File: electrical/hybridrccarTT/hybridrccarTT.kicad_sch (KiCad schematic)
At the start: 0 parts

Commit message: river the goat
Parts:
- added U1: STM32F103C8Tx, Package_QFP:LQFP-48_7x7mm_P0.5mm, symbol MCU_ST_STM32F1:STM32F103C8Tx
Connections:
- new net: U1.23 (VSS), U1.35 (VSS), U1.47 (VSS)
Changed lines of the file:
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@@
+		)
+	)
+	(symbol
+		(lib_id "MCU_ST_STM32F1:STM32F103C8Tx")
+		(at 76.2 97.79 0)
+		(unit 1)
+		(exclude_from_sim no)
+		(in_bom yes)
+		(on_board yes)
+		(dnp no)
+		(fields_autoplaced yes)
+		(property "Reference" "U1"
+			(at 80.8833 138.43 0)
+			(effects
+				(font
+					(size 1.27 1.27)
+				)
+				(justify left)
+			)
+		)
+		(property "Value" "STM32F103C8Tx"
+			(at 80.8833 140.97 0)
+			(effects
+				(font
+					(size 1.27 1.27)
+				)
+				(justify left)
+			)
+		)
+		(property "Footprint" "Package_QFP:LQFP-48_7x7mm_P0.5mm"
+			(at 60.96 135.89 0)
+			(effects
+				(font
+					(size 1.27 1.27)
+				)
+				(justify right)
+				(hide yes)
+			)
+		)
+		(property "Datasheet" "https://www.st.com/resource/en/datasheet/stm32f103c8.pdf"
+			(at 76.2 97.79 0)
+			(effects
+				(font
+					(size 1.27 1.27)
+				)
+				(hide yes)
+			)
+		)
+		(property "Description" "STMicroelectronics Arm Cortex-M3 MCU, 64KB flash, 20KB RAM, 72 MHz, 2.0-3.6V, 37 GPIO, LQFP48"
+			(at 76.2 97.79 0)
+			(effects
+				(font
+					(size 1.27 1.27)
+				)
+				(hide yes)
+			)
+		)
+		(pin "16"
+		)
+		(pin "15"
+		)
+		(pin "14"
+		)
+		(pin "13"
+		)
+		(pin "12"
+		)
+		(pin "11"
+		)
+		(pin "10"
+		)
+		(pin "34"
+		)
+		(pin "33"
+		)
+		(pin "32"
+		)
+		(pin "31"
+		)
+		(pin "30"
+		)
+		(pin "9"
+		)
+		(pin "47"
+		)
+		(pin "48"
+		)
+		(pin "8"
+		)
+		(pin "29"
+		)
+		(pin "17"
+		)
+		(pin "37"
+		)
+		(pin "38"
+		)
+		(pin "43"
+		)
+		(pin "45"
+		)
+		(pin "46"
+		)
+		(pin "3"
+		)
+		(pin "4"
+		)
+		(pin "18"
+		)
+		(pin "19"
+		)
+		(pin "20"
+		)
+		(pin "39"
+		)
+		(pin "40"
+		)
+		(pin "41"
+		)
+		(pin "1"
+		)
+		(pin "28"
+		)
+		(pin "27"
+		)
+		(pin "26"
+		)
+		(pin "25"
+		)
+		(pin "22"
+		)
+		(pin "21"
+		)
+		(pin "7"
+		)
+		(pin "44"
+		)
+		(pin "5"
+		)
+		(pin "6"
+		)
+		(pin "2"
+		)
+		(pin "42"
+		)
+		(pin "24"
+		)
+		(pin "36"
+		)
+		(pin "23"
+		)
+		(pin "35"
+		)
+		(instances
+			(project ""
+				(path "/d3b268c2-36da-438c-a1fa-ee4bf32aa038"
+					(reference "U1")
+					(unit 1)
+				)
+			)
 		)
 	)

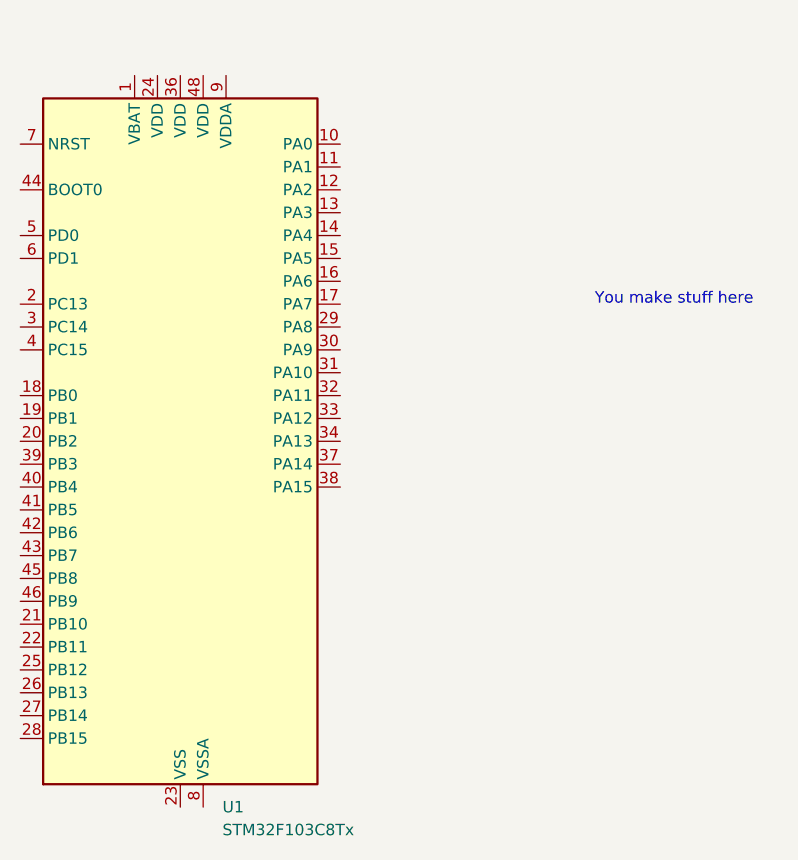
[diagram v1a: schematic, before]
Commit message: added stm32 lib
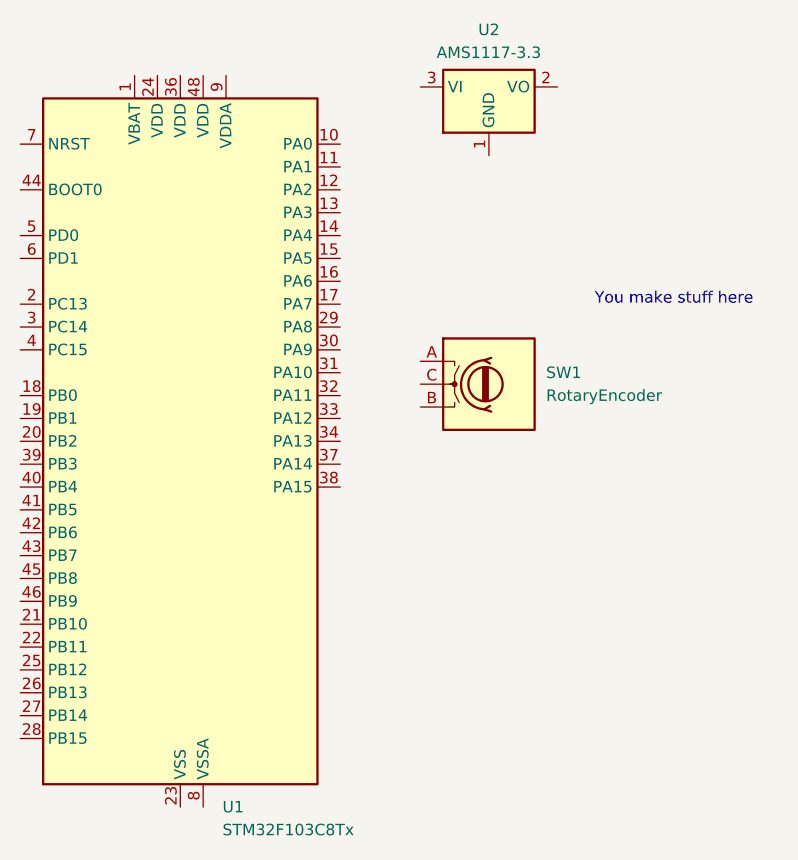
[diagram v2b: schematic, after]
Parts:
- added SW1: RotaryEncoder, symbol Device:RotaryEncoder
- added U2: AMS1117-3.3, Package_TO_SOT_SMD:SOT-223-3_TabPin2, symbol Regulator_Linear:AMS1117-3.3
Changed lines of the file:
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@@
+	)
+	(symbol
+		(lib_id "Device:RotaryEncoder")
+		(at 110.49 91.44 0)
+		(unit 1)
+		(exclude_from_sim no)
+		(in_bom yes)
+		(on_board yes)
+		(dnp no)
+		(fields_autoplaced yes)
+		(property "Reference" "SW1"
+			(at 116.84 90.1699 0)
+			(effects
+				(font
+					(size 1.27 1.27)
+				)
+				(justify left)
+			)
+		)
+		(property "Value" "RotaryEncoder"
+			(at 116.84 92.7099 0)
+			(effects
+				(font
+					(size 1.27 1.27)
+				)
+				(justify left)
+			)
+		)
+		(property "Footprint" ""
+			(at 106.68 87.376 0)
+			(effects
+				(font
+					(size 1.27 1.27)
+				)
+				(hide yes)
+			)
+		)
+		(property "Datasheet" "~"
+			(at 110.49 84.836 0)
+			(effects
+				(font
+					(size 1.27 1.27)
+				)
+				(hide yes)
+			)
+		)
+		(property "Description" "Rotary encoder, dual channel, incremental quadrate outputs"
+			(at 110.49 91.44 0)
+			(effects
+				(font
+					(size 1.27 1.27)
+				)
+				(hide yes)
+			)
+		)
+		(pin "A"
+		)
+		(pin "B"
+		)
+		(pin "C"
+		)
+		(instances
+			(project ""
+				(path "/d3b268c2-36da-438c-a1fa-ee4bf32aa038"
+					(reference "SW1")
+					(unit 1)
+				)
+			)
+		)
+	)
+	(symbol
+		(lib_id "Regulator_Linear:AMS1117-3.3")
+		(at 110.49 58.42 0)
+		(unit 1)
+		(exclude_from_sim no)
+		(in_bom yes)
+		(on_board yes)
+		(dnp no)
+		(fields_autoplaced yes)
+		(property "Reference" "U2"
+			(at 110.49 52.07 0)
+			(effects
+				(font
+					(size 1.27 1.27)
+				)
+			)
+		)
+		(property "Value" "AMS1117-3.3"
+			(at 110.49 54.61 0)
+			(effects
+				(font
+					(size 1.27 1.27)
+				)
+			)
+		)
+		(property "Footprint" "Package_TO_SOT_SMD:SOT-223-3_TabPin2"
+			(at 110.49 53.34 0)
+			(effects
+				(font
+					(size 1.27 1.27)
+				)
+				(hide yes)
+			)
+		)
+		(property "Datasheet" "http://www.advanced-monolithic.com/pdf/ds1117.pdf"
+			(at 113.03 64.77 0)
+			(effects
+				(font
+					(size 1.27 1.27)
+				)
+				(hide yes)
+			)
+		)
+		(property "Description" "1A Low Dropout regulator, positive, 3.3V fixed output, SOT-223"
+			(at 110.49 58.42 0)
+			(effects
+				(font
+					(size 1.27 1.27)
+				)
+				(hide yes)
+			)
+		)
+		(pin "3"
+		)
+		(pin "2"
+		)
+		(pin "1"
+		)
+		(instances
+			(project ""
+				(path "/d3b268c2-36da-438c-a1fa-ee4bf32aa038"
+					(reference "U2")
+					(unit 1)
+				)
+			)
+		)
 	)
 	(symbol
